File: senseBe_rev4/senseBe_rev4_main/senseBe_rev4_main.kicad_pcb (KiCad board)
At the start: 2 copper layers, 56.5 x 40 mm, 62 parts, among them J1 PJ-611-5A_AudioJack, J2 Conn_02x03_Odd_Even, Q1 SI2302, Q2 Q_PMOS_GDS, Q4 SI2302, Q5 SI2302, Q6 SI2302, Q7 SI2302, SW1 SW_Push_SPDT, SW2 SW_SPST, U1 MDBT42Q, U2 TSSP4056, U3 AP3405, U4 PCF8563T, Y1 Crystal, Y2 Q13FC1350000400

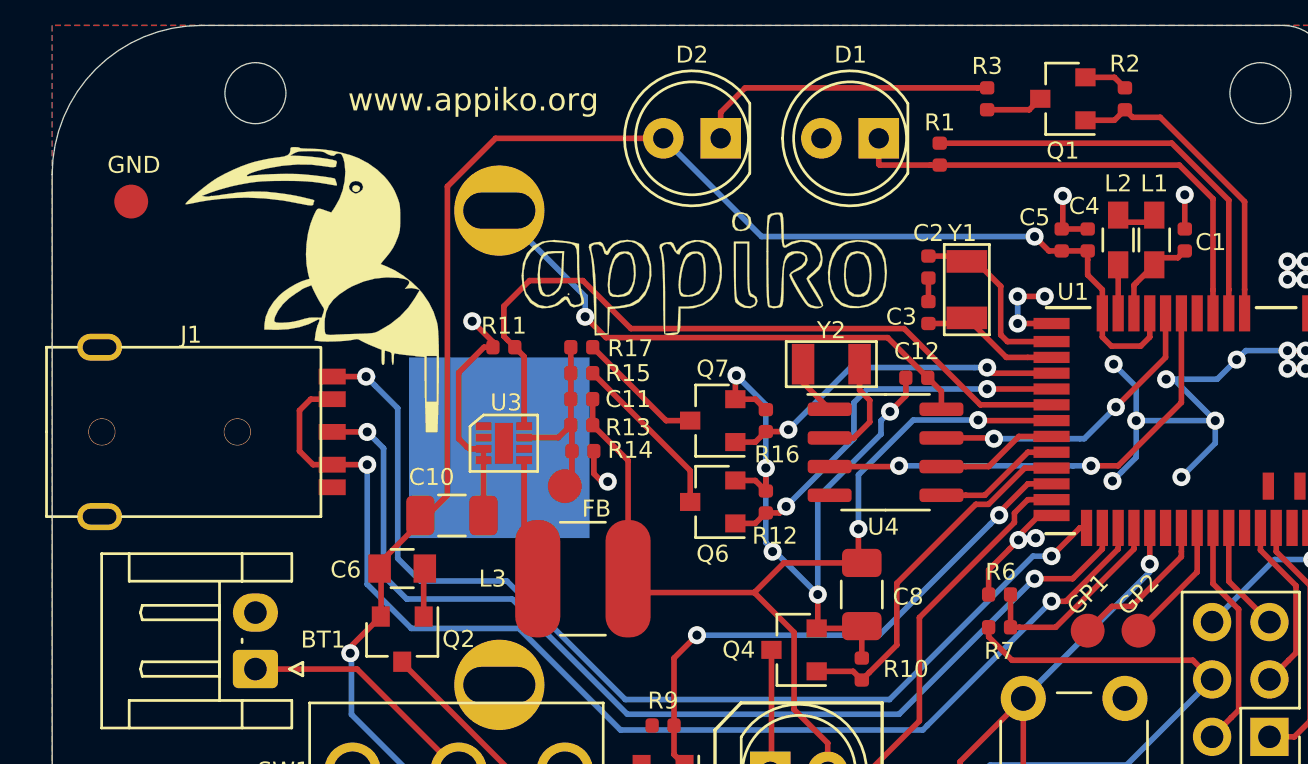
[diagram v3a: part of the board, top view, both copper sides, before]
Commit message: fix in schematic and gerber files regenerated.
VDD to Buck regulator connection was missing.
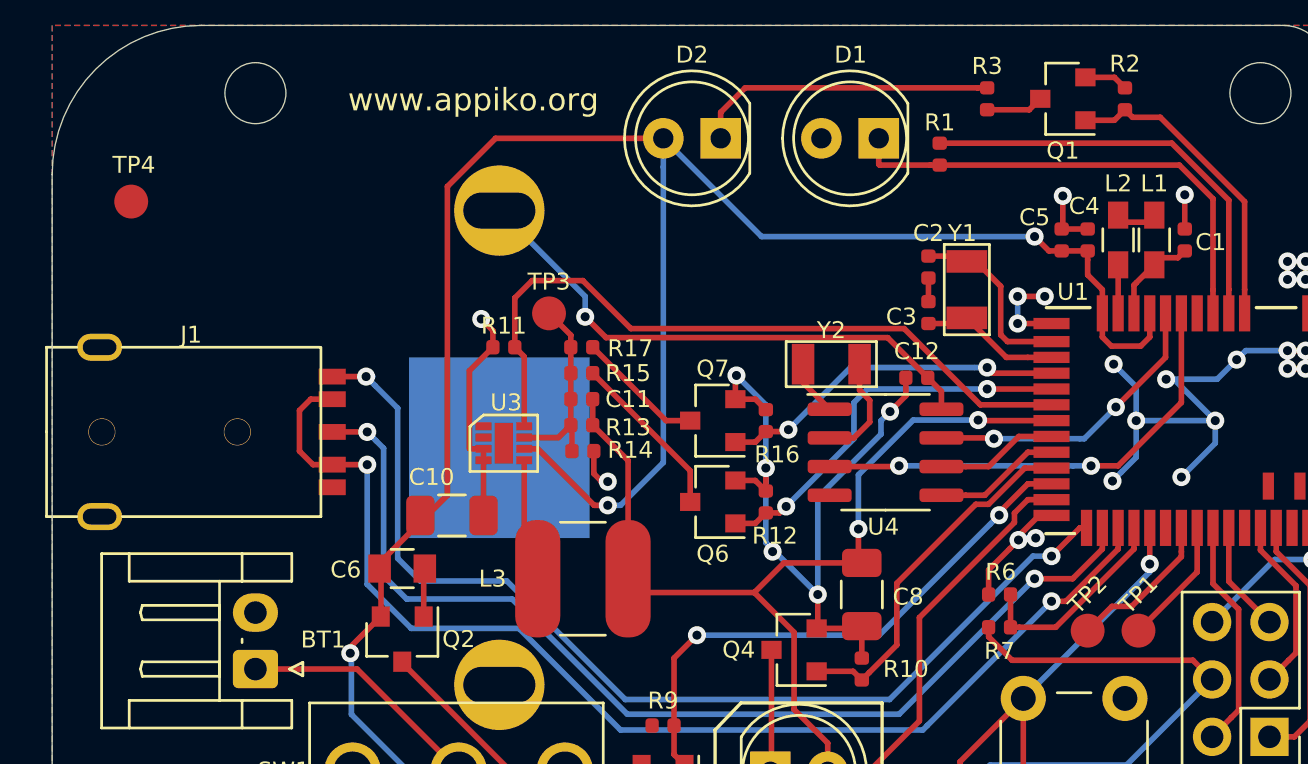
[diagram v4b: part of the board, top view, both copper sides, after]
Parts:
- removed G***: LOGO, sense_fp:OSHW1
- removed G***: Appiko_Logo_2, sense_fp:Appiko_Logo_2
- removed G***: Appiko_LOGO_img, sense_fp:Appiko_LOGO_img
- moved TP3 7.68 mm to (32.0, 22.8)
- renumbered GP2 to TP1, GP1 to TP2, FB to TP3, GND to TP4
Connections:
- U3 pad 6: Net-(U3-Pad6) -> VDD
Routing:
- net VDD: track 128.0 -> 150.3 mm, vias 2 -> 3
- net GND: track 108.6 -> 107.9 mm

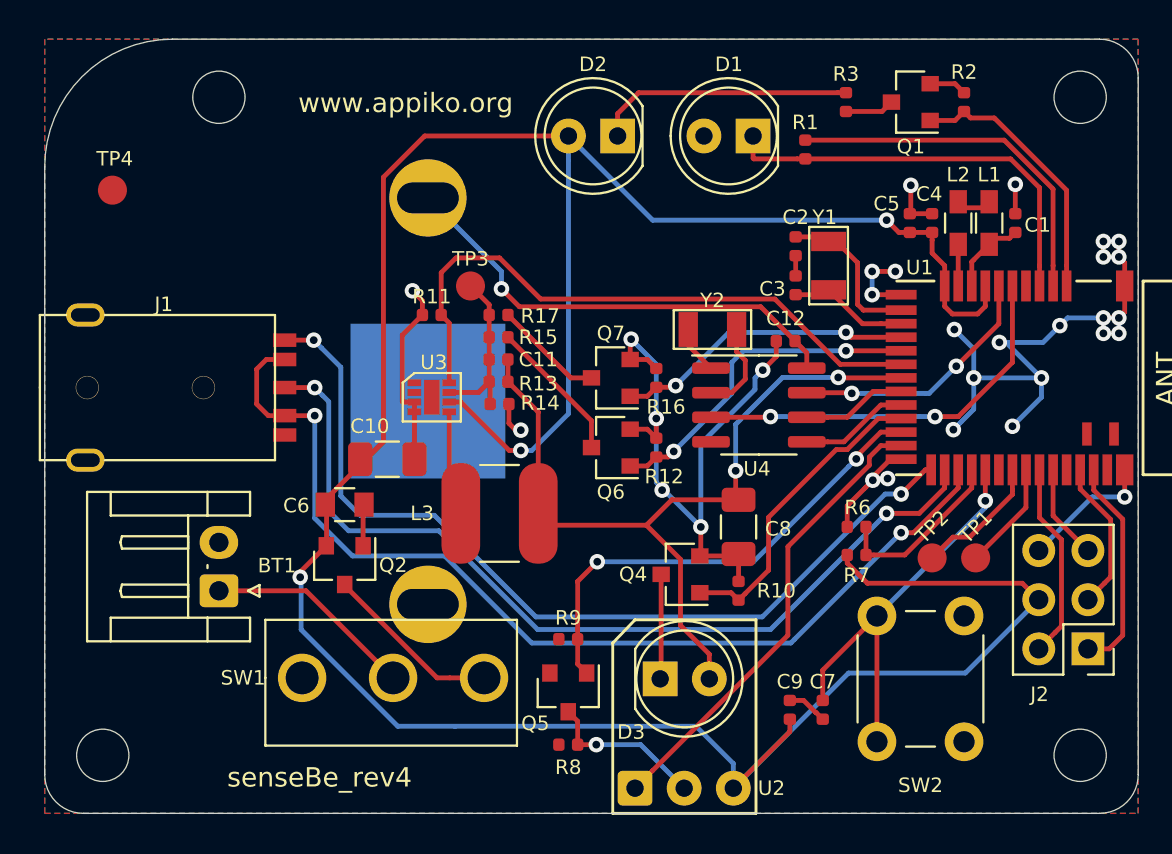
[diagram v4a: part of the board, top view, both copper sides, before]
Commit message: LED and LDR positions changed on PCB.
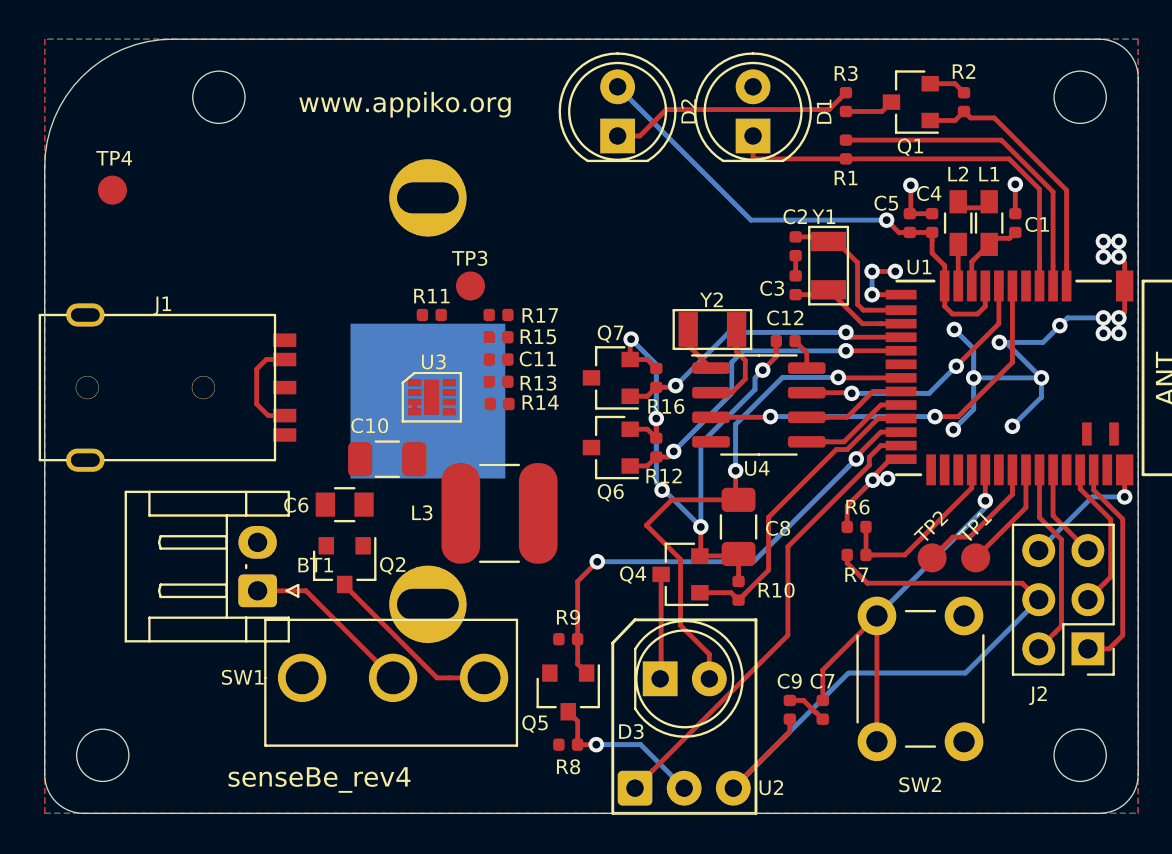
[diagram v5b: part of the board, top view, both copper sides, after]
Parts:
- moved R1 2.10 mm to (51.4, 15.7)
- moved BT1 2.00 mm to (21.0, 38.5)
- turned D1 to 90 degrees
- turned D2 to 90 degrees
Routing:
- net VDD: track 150.3 -> 62.7 mm, vias 3 -> 1
- net /FOCUS: track 52.4 -> 5.41 mm, vias 2 -> 0
- net /TRIGGER: track 46.7 -> 0.00 mm, vias 2 -> 0
- net /CAM_JACK: track 46.6 -> 0.00 mm, vias 2 -> 0
- net /REG_EN: track 32.2 -> 0.00 mm
- net Net-(BT2-Pad1): track 24.2 -> 1.65 mm, vias 1 -> 0
- net /VLED: track 42.6 -> 28.1 mm
- net GND: track 107.9 -> 94.6 mm, vias 30 -> 28
- net Net-(C11-Pad2): track 8.81 -> 0.00 mm
- net Net-(Q6-Pad3): track 7.49 -> 0.00 mm
- net Net-(Q7-Pad3): track 5.66 -> 0.00 mm
- net Net-(L3-Pad1): track 5.50 -> 0.00 mm
- net /LIGHT_SENSE_EN: track 18.9 -> 16.7 mm
- net Net-(BT1-Pad1): track 10.9 -> 8.86 mm
- net Net-(D2-Pad1): track 13.4 -> 12.7 mm

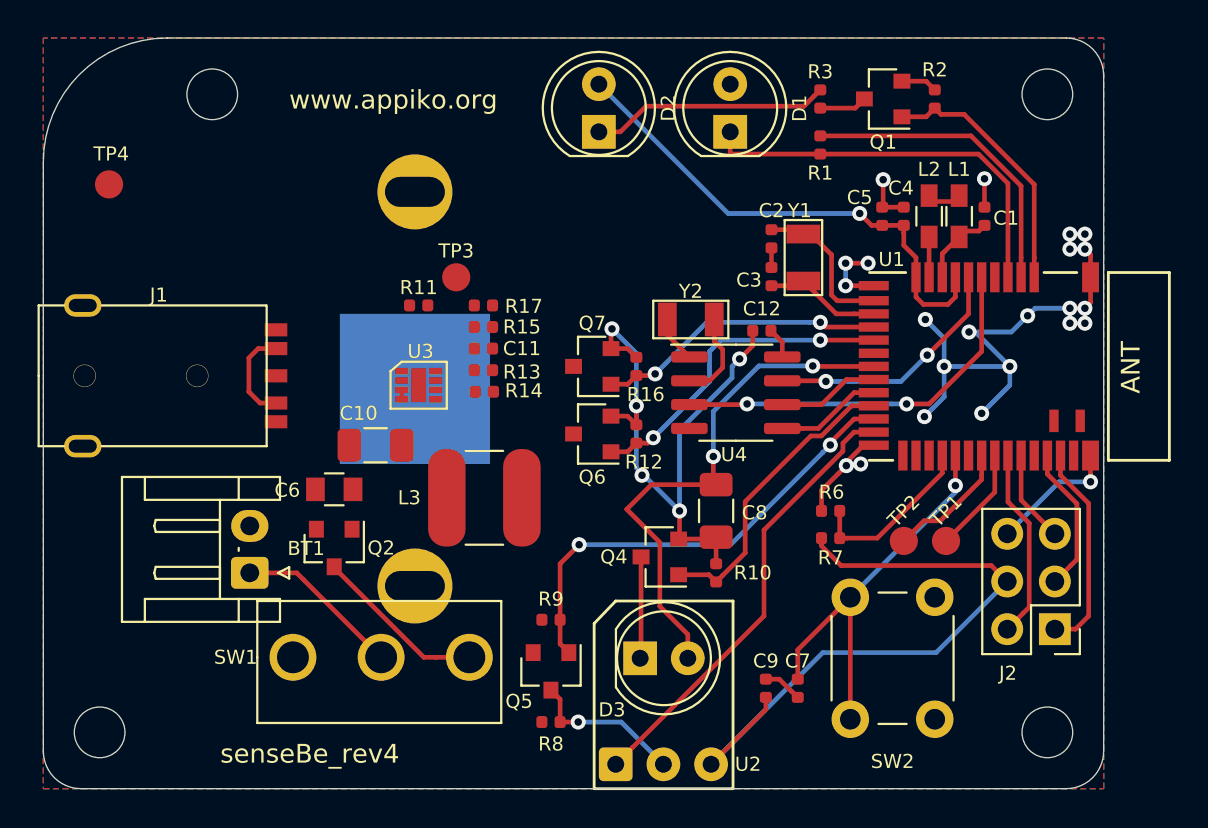
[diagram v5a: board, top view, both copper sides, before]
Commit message: Revamped SenseBe rev4 with fixes to the LED LDR placement
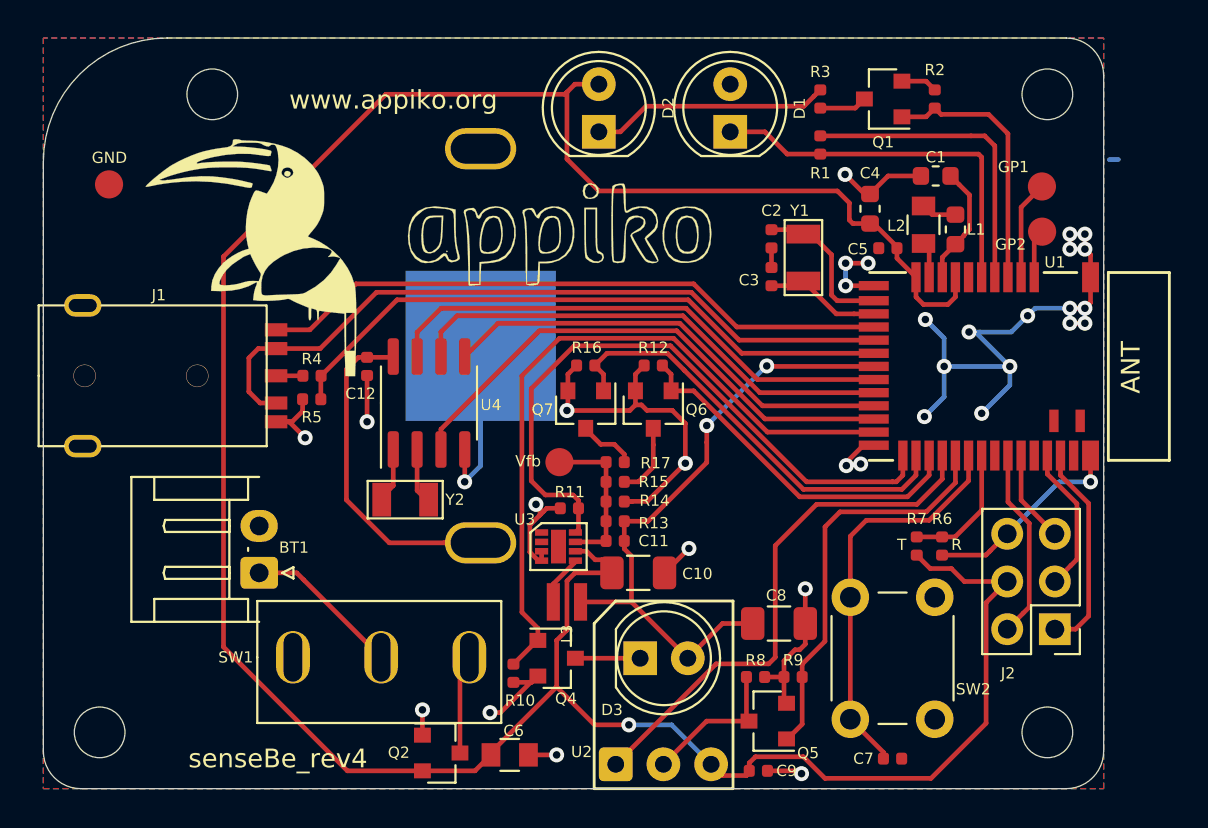
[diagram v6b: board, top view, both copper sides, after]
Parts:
- added G***: LOGO, sense_fp:OSHW1, B.Cu at (57.9, 21.3)
- added G***: Appiko_Logo_2, sense_fp:Appiko_Logo_2, F.Cu at (35.2, 20.5)
- added G***: Appiko_LOGO_img, sense_fp:Appiko_LOGO_img, F.Cu at (21.1, 21.7)
- added R4: 470E, sense_fp:C_0402_1005Metric, F.Cu at (24.3, 28.0)
- added R5: 1.2k, sense_fp:C_0402_1005Metric, F.Cu at (24.3, 29.2)
- C1, C4: footprint sense_fp:C_0402_1005Metric -> sense_fp:C_0603_1608Metric
- L1: value 15nH -> 18nH; footprint sense_fp:L_0603_HandSoldering -> sense_fp:C_0603_1608Metric
- L2: value 10nH -> 10uH; footprint sense_fp:L_0603_HandSoldering -> sense_fp:C_0805
- L3: footprint sense_fp:L_5mm_SMD_copy -> sense_fp:L_2.4mm_SMD
- Q2: value Q_PMOS_GDS -> IRLML6401
- moved C12 21.1 mm to (27.2, 27.5), turned to 90 degrees
- moved GP1 19.6 mm to (63.2, 17.9)
- moved GP2 18.1 mm to (63.2, 20.3)
- moved Y2 18.0 mm to (29.3, 34.6)
- moved C6 17.0 mm to (34.9, 48.2)
- moved U4 16.4 mm to (30.6, 29.4), turned to 90 degrees
- moved C10 15.6 mm to (41.7, 38.5)
- moved R11 13.5 mm to (38.0, 35.1)
- moved R9 13.3 mm to (50.0, 44.0)
- moved C11 12.4 mm to (40.5, 36.8)
- moved Q2 12.3 mm to (31.2, 48.1), turned to 0 degrees
- moved R10 12.1 mm to (35.0, 43.9), turned to 270 degrees
- moved Q5 11.9 mm to (48.6, 46.4), turned to 180 degrees
- moved U3 11.4 mm to (37.5, 37.1)
- moved Vfb 11.3 mm to (37.5, 32.6)
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- renumbered TP4 to GND, TP1 to GP1, TP2 to GP2, TP3 to Vfb
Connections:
- J1 pad 3: /CAM_JACK -> Net-(J1-Pad3)
- SW1 pad 1: GND -> Net-(SW1-Pad1)
- U1 pad 15: /PWR2 -> /TRIGGER
- U1 pad 16: /PWR1 -> /FOCUS
- U1 pad 17: /REG_EN -> /CAM_JACK
- U1 pad 19: /SCL -> /RTC_CLK
- U1 pad 2: /LED_RED -> /GPIO2
- U1 pad 20: /SDA -> /SCL
- U1 pad 21: /IR_LED_EN -> /SDA
- U1 pad 22: /RX_EN -> /RTC_INT
- U1 pad 23: /RX_OUT -> /IR_LED_EN
- U1 pad 25: /TRIGGER -> /REG_EN
- U1 pad 26: /CAM_JACK -> /PWR2
- U1 pad 27: /FOCUS -> /PWR1
- U1 pad 28: /RX_TX_S -> /RX_OUT
- U1 pad 29: /BUTTON -> /RX_EN
- U1 pad 3: /LIGHT_SENSE_EN -> /GPIO1
- U1 pad 30: Net-(U1-Pad30) -> /BUTTON
- U1 pad 31: /GPIO2 -> /RX_TX_S
- U1 pad 32: /GPIO1 -> Net-(U1-Pad32)
- U1 pad 4: /LIGHT_SENSE -> /LED_RED
- U1 pad 5: Net-(U1-Pad5) -> /LIGHT_SENSE_EN
- U1 pad 6: /RTC_INT -> /LIGHT_SENSE
- U1 pad 7: /RTC_CLK -> Net-(U1-Pad7)
- U4 pad 4: Net-(U4-Pad4) -> GND
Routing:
- net VDD: track 62.7 -> 149.0 mm
- net /REG_EN: track 0.00 -> 34.6 mm
- net /FOCUS: track 5.41 -> 39.6 mm
- net /TRIGGER: track 0.00 -> 33.8 mm
- net /CAM_JACK: track 0.00 -> 33.6 mm
- net /IR_LED_EN: track 16.0 -> 37.9 mm
- net /SCL: track 5.43 -> 26.4 mm
- net GND: track 94.6 -> 115.0 mm, vias 28 -> 34
- net /SDA: track 5.66 -> 24.4 mm
- net Net-(BT2-Pad1): track 1.65 -> 17.9 mm
- net /RTC_CLK: track 13.4 -> 27.7 mm, vias 2 -> 0
- net Net-(C11-Pad2): track 0.00 -> 8.34 mm
- net /PWR2: track 15.5 -> 23.3 mm, vias 2 -> 0
- net /RTC_INT: track 20.7 -> 28.3 mm, vias 2 -> 0
- net /VLED: track 28.1 -> 33.5 mm
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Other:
- board text added: "R"
- board text added: "T"

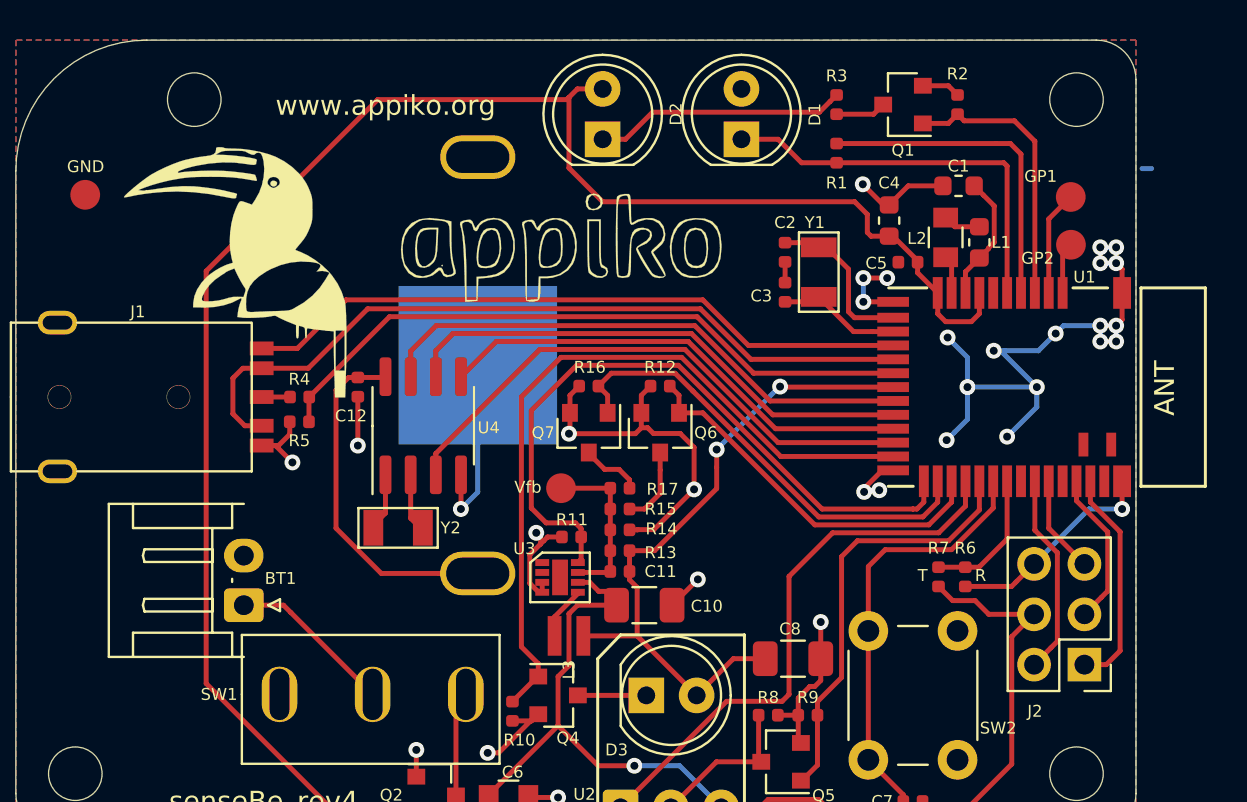
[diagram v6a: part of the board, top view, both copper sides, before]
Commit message: Update SenseBe rev4 with minor fixes
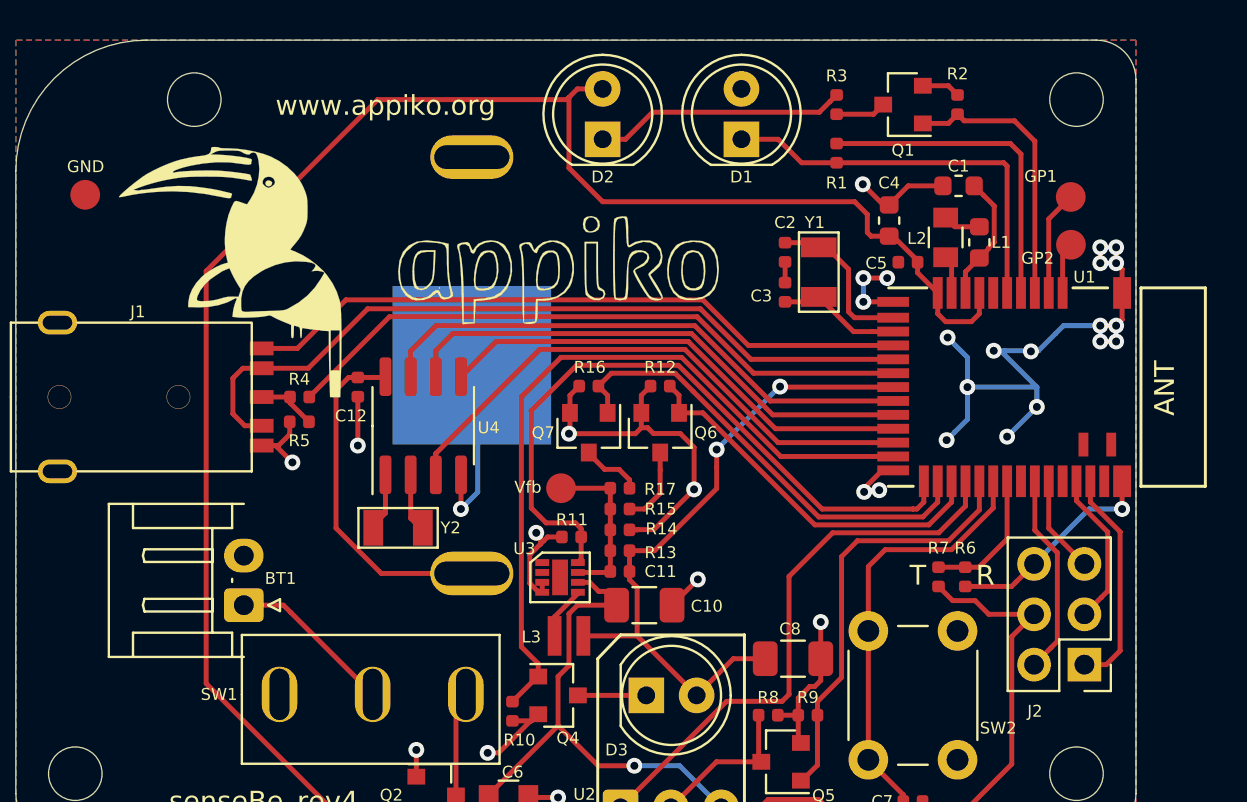
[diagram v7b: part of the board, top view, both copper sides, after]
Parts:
- L3: value 22uH -> 2.2uH
- R17: value 1.2M -> 1M
- R5: value 1.2k -> NC
- moved G*** 2.91 mm to (55.7, 19.4)
- moved G*** 1.14 mm to (35.1, 21.6)
- moved BT2 0.30 mm to (33.0, 26.4)
- moved G*** 0.25 mm to (20.8, 21.7)
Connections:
- R5 pad 1: /CAM_JACK -> Net-(J1-Pad3)
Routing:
- net Net-(J1-Pad3): track 1.43 -> 3.08 mm
- net /CAM_JACK: track 33.6 -> 32.3 mm
